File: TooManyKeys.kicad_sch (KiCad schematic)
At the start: 5 parts, among them J1 LCD Conn (1x8 PicoBlade), J2 BOOSTIER, SW1 SW_SPDT, SW2 SW_RST, U1 Nice_Nano_V2

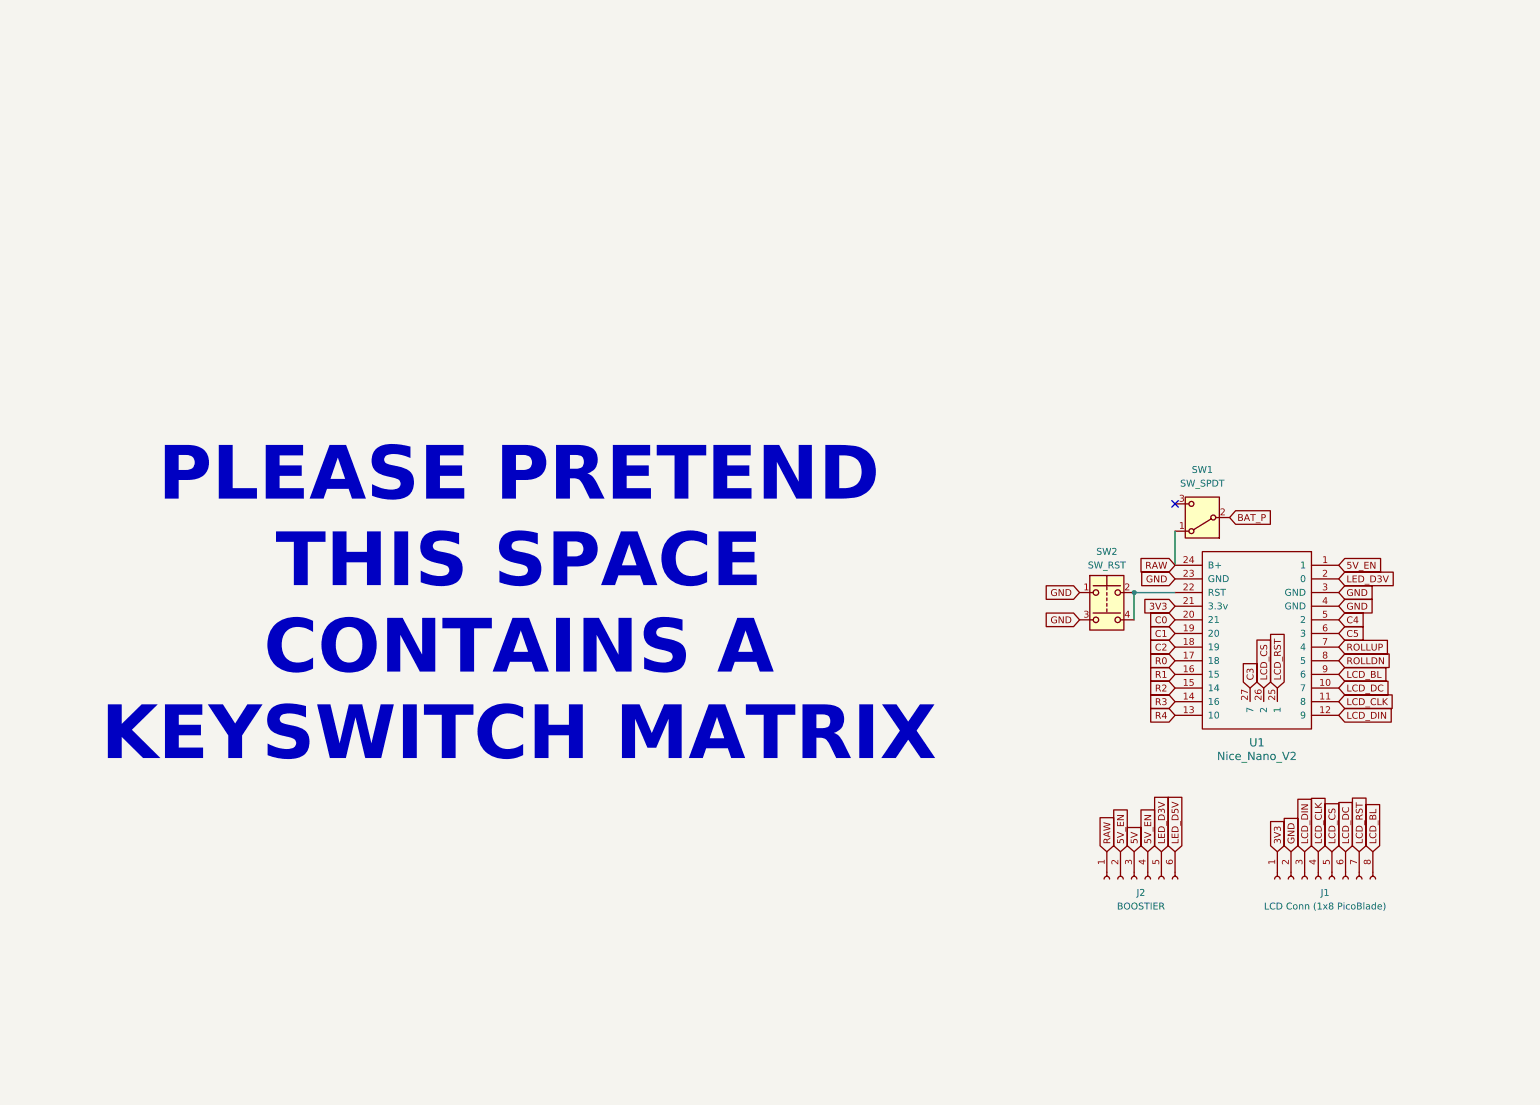
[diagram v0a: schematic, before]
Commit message: Finish schematic. Partial routing draft. Minor changes to via sizes in ergogen.
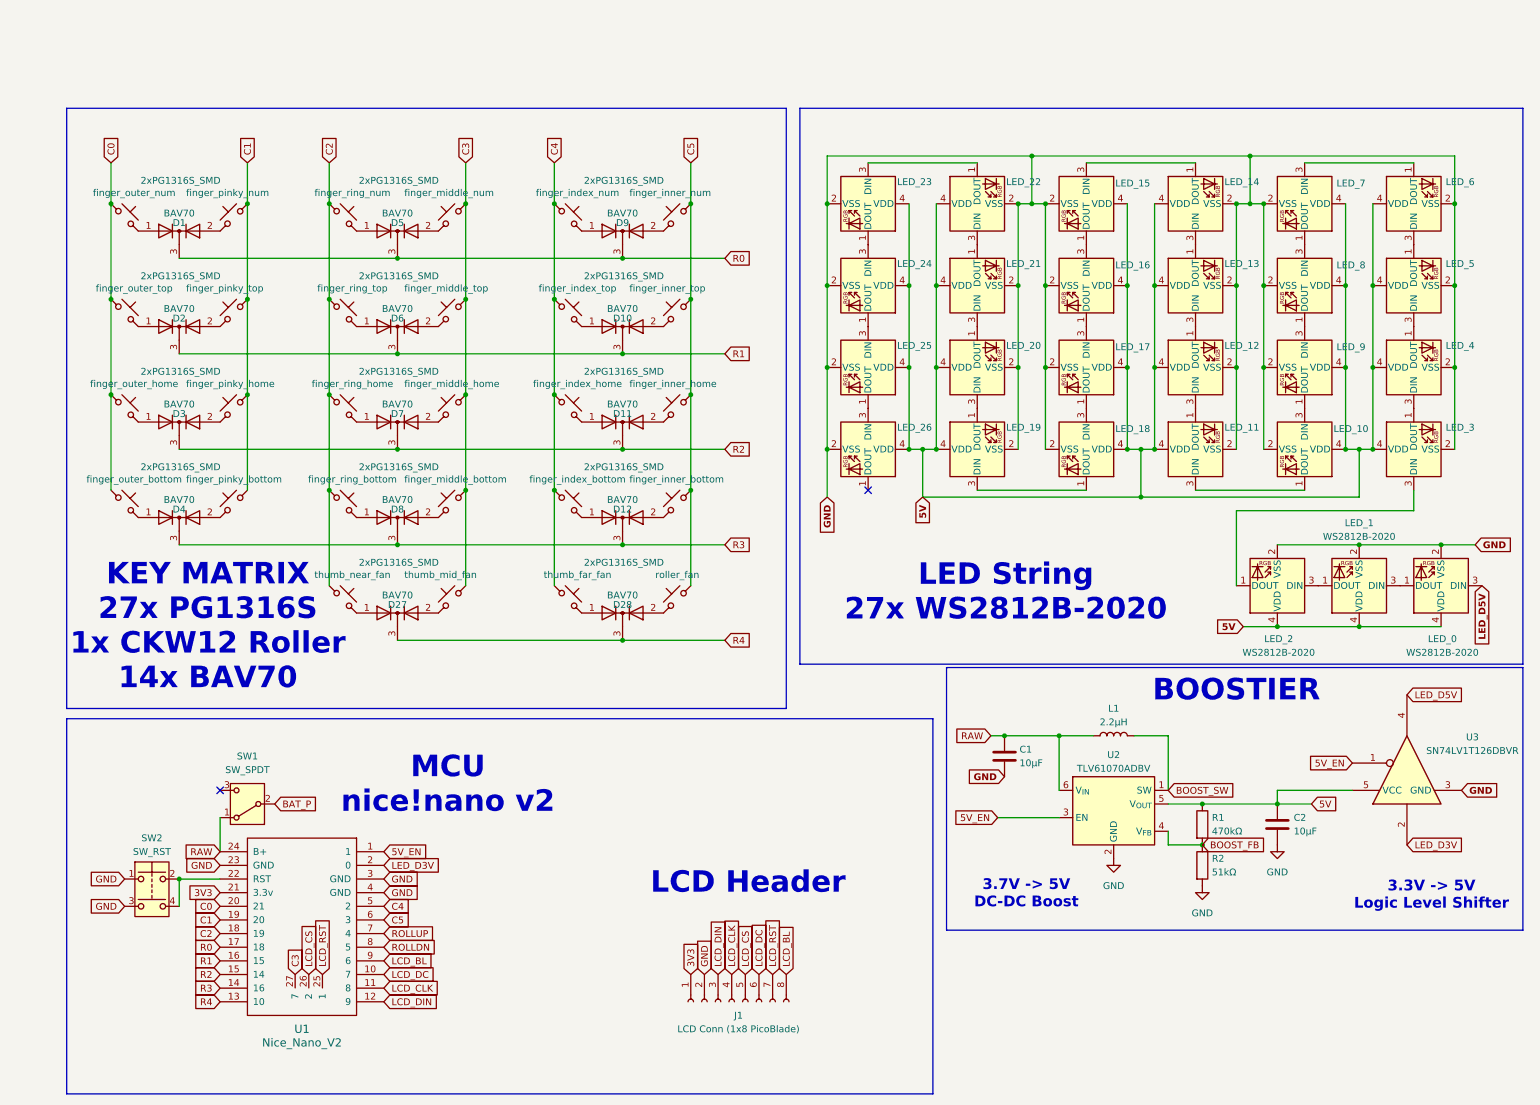
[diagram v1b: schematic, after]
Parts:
- removed J2: BOOSTIER, symbol Connector:Conn_01x06_Socket
- added C1, C2: 10μF, Capacitor_SMD:C_0603_1608Metric, symbol Device:C
- added D1, D10, D11, D12, D2, D27, D28, D3, D4, D5, D6, D7, D8, D9: BAV70, Package_TO_SOT_SMD:SOT-23, symbol Diode:BAV70
- added L1: 2.2μH, huntercook:L_CJIANG_FTC404030S_4.1x4.1x3.0_SMD, symbol Device:L
- added LED_0, LED_1, LED_10, LED_11, LED_12, LED_13, LED_14, LED_15, LED_16, LED_17, LED_18, LED_19, LED_2, LED_20, LED_21, LED_22, LED_23, LED_24, LED_25, LED_26, LED_3, LED_4, LED_5, LED_6, LED_7, LED_8, LED_9: WS2812B-2020, LED_SMD:LED_WS2812B-2020_PLCC4_2.0x2.0mm, symbol LED:WS2812B-2020
- added R1: 470kΩ, Resistor_SMD:R_0603_1608Metric, symbol Device:R
- added R2: 51kΩ, Resistor_SMD:R_0603_1608Metric, symbol Device:R
- added U2: TLV61070ADBV, Package_TO_SOT_SMD:SOT-23-6, symbol Regulator_Switching:TLV61070ADBV
- added U3: SN74LV1T126DBVR, Package_TO_SOT_SMD:SOT-23-5, symbol 74xGxx:SN74LVC1G125DBV
- added finger_index_bottom, finger_index_home, finger_index_num, finger_index_top, finger_outer_bottom, finger_outer_home, finger_outer_num, finger_outer_top, finger_ring_bottom, finger_ring_home, finger_ring_num, finger_ring_top, thumb_far_fan, thumb_near_fan: 2xPG1316S_SMD, PCM_marbastlib-choc:SW_choc_v1_1u, symbol marbastlib-choc:choc_v1_SW_solder
- added finger_inner_bottom, finger_inner_home, finger_inner_num, finger_inner_top, finger_middle_bottom, finger_middle_home, finger_middle_num, finger_middle_top, finger_pinky_bottom, finger_pinky_home, finger_pinky_num, finger_pinky_top, roller_fan, thumb_mid_fan: PG1316S_SMD, PCM_marbastlib-choc:SW_choc_v1_1u, symbol marbastlib-choc:choc_v1_SW_solder
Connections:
- net 5V: now also C2.1, LED_0.4 (VDD), LED_1.4 (VDD), LED_10.4 (VDD), LED_11.4 (VDD), LED_12.4 (VDD), LED_13.4 (VDD), LED_14.4 (VDD), LED_15.4 (VDD), LED_16.4 (VDD), LED_17.4 (VDD), LED_18.4 (VDD), LED_19.4 (VDD), LED_2.4 (VDD), LED_20.4 (VDD), LED_21.4 (VDD), LED_22.4 (VDD), LED_23.4 (VDD), LED_24.4 (VDD), LED_25.4 (VDD), LED_26.4 (VDD), LED_3.4 (VDD), LED_4.4 (VDD), LED_5.4 (VDD), LED_6.4 (VDD), LED_7.4 (VDD), LED_8.4 (VDD), LED_9.4 (VDD), R1.1, U2.5 (V_{OUT}), U3.5 (VCC)
- net 5V_EN: now also U2.3 (EN), U3.1
- net C0: now also finger_outer_bottom.1, finger_outer_home.1, finger_outer_num.1, finger_outer_top.1
- net C1: now also finger_pinky_bottom.2, finger_pinky_home.2, finger_pinky_num.2, finger_pinky_top.2
- net C2: now also finger_ring_bottom.1, finger_ring_home.1, finger_ring_num.1, finger_ring_top.1, thumb_near_fan.1
- net C3: now also finger_middle_bottom.2, finger_middle_home.2, finger_middle_num.2, finger_middle_top.2, thumb_mid_fan.2
- net C4: now also finger_index_bottom.1, finger_index_home.1, finger_index_num.1, finger_index_top.1, thumb_far_fan.1
- net C5: now also finger_inner_bottom.2, finger_inner_home.2, finger_inner_num.2, finger_inner_top.2, roller_fan.2
- net GND: now also C1.2, C2.2, LED_0.2 (VSS), LED_1.2 (VSS), LED_10.2 (VSS), LED_11.2 (VSS), LED_12.2 (VSS), LED_13.2 (VSS), LED_14.2 (VSS), LED_15.2 (VSS), LED_16.2 (VSS), LED_17.2 (VSS), LED_18.2 (VSS), LED_19.2 (VSS), LED_2.2 (VSS), LED_20.2 (VSS), LED_21.2 (VSS), LED_22.2 (VSS), LED_23.2 (VSS), LED_24.2 (VSS), LED_25.2 (VSS), LED_26.2 (VSS), LED_3.2 (VSS), LED_4.2 (VSS), LED_5.2 (VSS), LED_6.2 (VSS), LED_7.2 (VSS), LED_8.2 (VSS), LED_9.2 (VSS), R2.2, U2.2 (GND), U3.3 (GND)
- net LED_D3V: now also U3.2
- net LED_D5V: now also LED_0.3 (DIN), U3.4
- net R0: now also D1.3 (K), D5.3 (K), D9.3 (K)
- net R1: now also D10.3 (K), D2.3 (K), D6.3 (K)
- net R2: now also D11.3 (K), D3.3 (K), D7.3 (K)
- net R3: now also D12.3 (K), D4.3 (K), D8.3 (K)
- net R4: now also D27.3 (K), D28.3 (K)
- net RAW: now also C1.1, L1.1, U2.6 (V_{IN})
- new net: D27.2 (A), thumb_mid_fan.1
- new net: D12.1 (A), finger_index_bottom.2
- new net: LED_19.1 (DOUT), LED_20.3 (DIN)
- new net: LED_18.1 (DOUT), LED_19.3 (DIN)
- new net: LED_11.1 (DOUT), LED_12.3 (DIN)
- new net: LED_10.1 (DOUT), LED_11.3 (DIN)
- new net: D7.1 (A), finger_ring_home.2
- new net: LED_6.1 (DOUT), LED_7.3 (DIN)
- new net: LED_5.1 (DOUT), LED_6.3 (DIN)
- new net: D2.1 (A), finger_outer_top.2
- new net: D2.2 (A), finger_pinky_top.1
- new net: D1.1 (A), finger_outer_num.2
- new net: D1.2 (A), finger_pinky_num.1
- new net: D3.1 (A), finger_outer_home.2
- new net: D3.2 (A), finger_pinky_home.1
- new net: LED_20.1 (DOUT), LED_21.3 (DIN)
- new net: D11.1 (A), finger_index_home.2
- new net: LED_12.1 (DOUT), LED_13.3 (DIN)
- new net: LED_1.1 (DOUT), LED_2.3 (DIN)
- new net: LED_0.1 (DOUT), LED_1.3 (DIN)
- new net: D12.2 (A), finger_inner_bottom.1
- new net: D8.1 (A), finger_ring_bottom.2
- new net: D8.2 (A), finger_middle_bottom.1
- new net: D10.1 (A), finger_index_top.2
- new net: LED_21.1 (DOUT), LED_22.3 (DIN)
- new net: D9.1 (A), finger_index_num.2
- new net: D7.2 (A), finger_middle_home.1
- new net: LED_4.1 (DOUT), LED_5.3 (DIN)
- new net: LED_3.1 (DOUT), LED_4.3 (DIN)
- new net: LED_22.1 (DOUT), LED_23.3 (DIN)
- new net: LED_24.1 (DOUT), LED_25.3 (DIN)
- new net: LED_23.1 (DOUT), LED_24.3 (DIN)
- new net: D9.2 (A), finger_inner_num.1
- new net: LED_2.1 (DOUT), LED_3.3 (DIN)
- new net: D4.1 (A), finger_outer_bottom.2
- new net: D28.1 (A), thumb_far_fan.2
- new net: D28.2 (A), roller_fan.1
- new net: D6.1 (A), finger_ring_top.2
- new net: LED_10.3 (DIN), LED_9.1 (DOUT)
- new net: LED_8.1 (DOUT), LED_9.3 (DIN)
- new net: D11.2 (A), finger_inner_home.1
- new net: D27.1 (A), thumb_near_fan.2
- new net: D5.1 (A), finger_ring_num.2
- new net: D5.2 (A), finger_middle_num.1
- new net: LED_7.1 (DOUT), LED_8.3 (DIN)
- new net: D4.2 (A), finger_pinky_bottom.1
- new net: LED_15.1 (DOUT), LED_16.3 (DIN)
- new net: LED_14.1 (DOUT), LED_15.3 (DIN)
- new net: LED_25.1 (DOUT), LED_26.3 (DIN)
- new net: LED_17.1 (DOUT), LED_18.3 (DIN)
- new net: LED_16.1 (DOUT), LED_17.3 (DIN)
- new net: D10.2 (A), finger_inner_top.1
- new net: D6.2 (A), finger_middle_top.1
- new net: LED_13.1 (DOUT), LED_14.3 (DIN)
- new net BOOST_FB: R1.2, R2.1, U2.4 (V_{FB})
- new net BOOST_SW: L1.2, U2.1 (SW)
- no-connect marks 1 -> 2
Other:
- note added: "3.3V -> 5V Logic Level Shifter"
- note added: "3.7V -> 5V DC-DC Boost"
- note added: "BOOSTIER"
- note added: "KEY MATRIX 27x PG1316S 1x CKW12 Roller 14x BAV70"
- note added: "LCD Header"
- note added: "LED String 27x WS2812B-2020"
- note added: "MCU nice!nano v2"
- note removed: "PLEASE PRETEND THIS SPACE CONTAINS A KEYSWITCH MATRIX"
- moved on the sheet: J1, SW1, SW2, U1

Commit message: Redo schematic references to match ergogen, work on connecting sch and pcb.
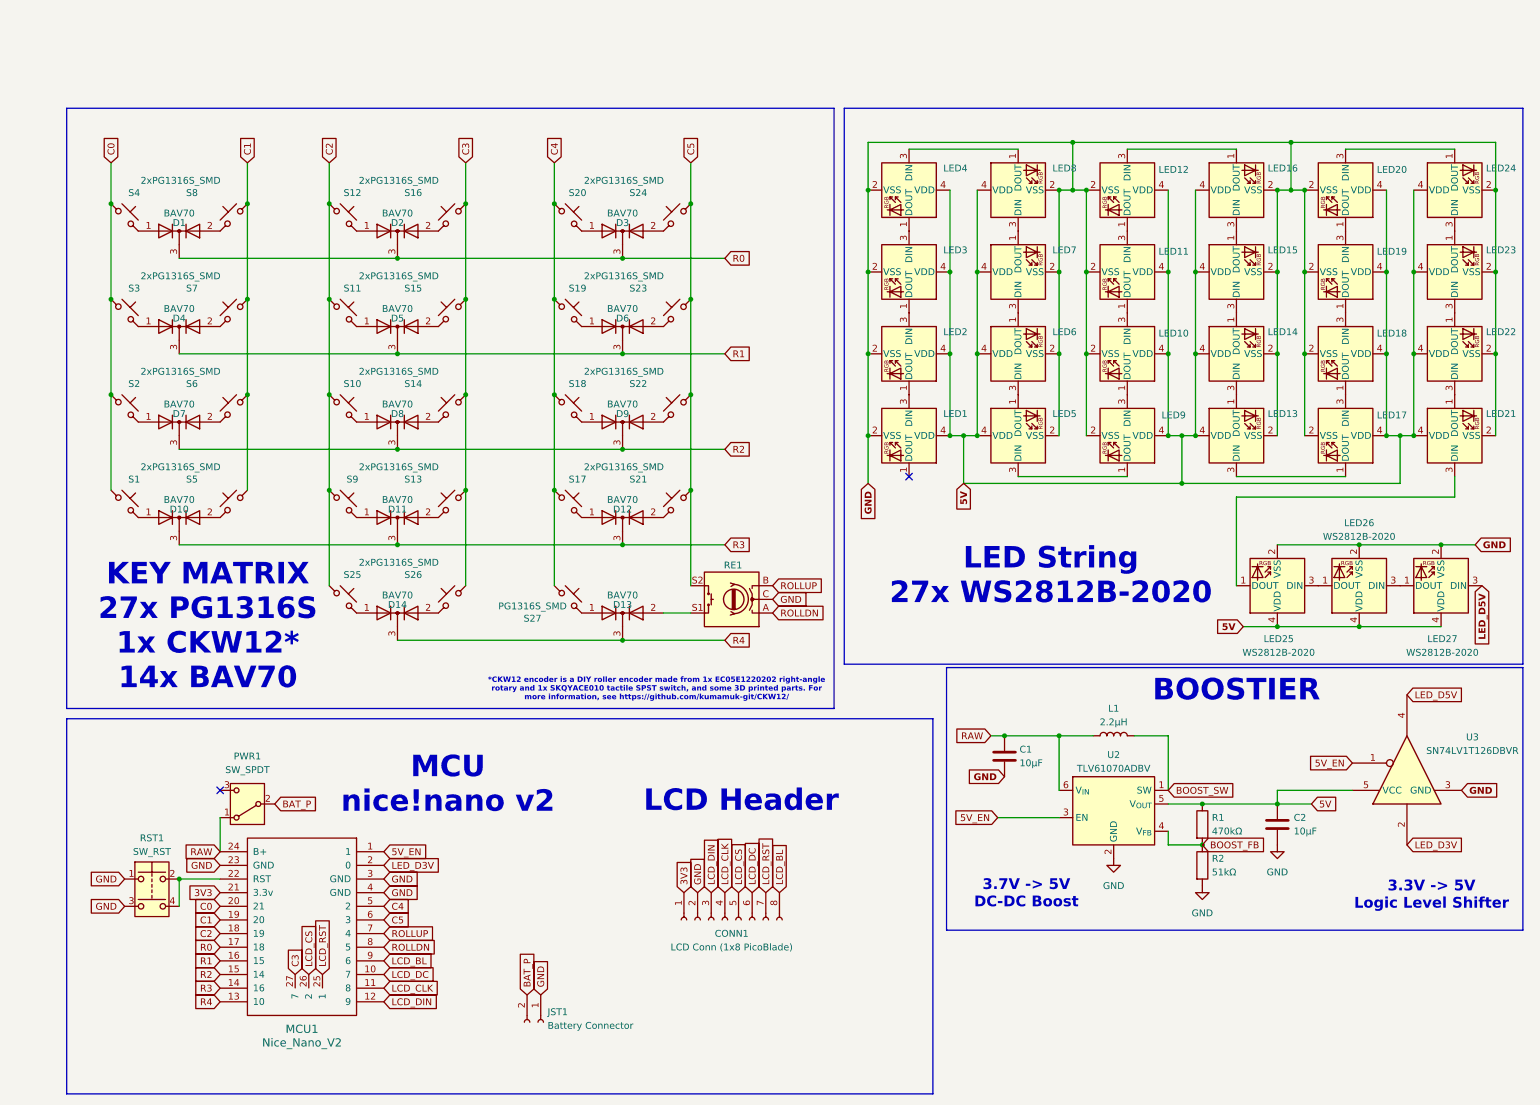
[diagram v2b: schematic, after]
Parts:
- removed roller_fan: PG1316S_SMD, PCM_marbastlib-choc:SW_choc_v1_1u, symbol marbastlib-choc:choc_v1_SW_solder
- added JST1: Battery Connector, symbol Connector:Conn_01x02_Socket
- added SW3: RE1, symbol Device:RotaryEncoder_Switch
- S27: renamed from thumb_far_fan; value 2xPG1316S_SMD -> PG1316S_SMD
- renumbered J1 to CONN1, D4 to D10, D8 to D11, D28 to D13, D27 to D14, D5 to D2, D9 to D3, D2 to D4, D6 to D5, D10 to D6, D3 to D7, D7 to D8, D11 to D9, LED_26 to LED1, LED_17 to LED10, LED_16 to LED11, LED_15 to LED12, LED_11 to LED13, LED_12 to LED14, LED_13 to LED15, LED_14 to LED16, LED_10 to LED17, LED_9 to LED18, LED_8 to LED19, LED_25 to LED2, LED_7 to LED20, LED_3 to LED21, LED_4 to LED22, LED_5 to LED23, LED_6 to LED24, LED_2 to LED25, LED_1 to LED26, LED_0 to LED27, LED_24 to LED3, LED_23 to LED4, LED_19 to LED5, LED_20 to LED6, LED_21 to LED7, LED_22 to LED8, LED_18 to LED9, U1 to MCU1, SW1 to PWR1, SW2 to RST1, finger_outer_bottom to S1, finger_ring_home to S10, finger_ring_top to S11, finger_ring_num to S12, finger_middle_bottom to S13, finger_middle_home to S14, finger_middle_top to S15, finger_middle_num to S16, finger_index_bottom to S17, finger_index_home to S18, finger_index_top to S19, finger_outer_home to S2, finger_index_num to S20, finger_inner_bottom to S21, finger_inner_home to S22, finger_inner_top to S23, finger_inner_num to S24, thumb_near_fan to S25, thumb_mid_fan to S26, finger_outer_top to S3, finger_outer_num to S4, finger_pinky_bottom to S5, finger_pinky_home to S6, finger_pinky_top to S7, finger_pinky_num to S8, finger_ring_bottom to S9
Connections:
- net BAT_P: now also JST1.2 (Pin_2)
- net C5: now also SW3.S2
- net GND: now also JST1.1 (Pin_1), SW3.C
- net ROLLDN: now also SW3.A
- net ROLLUP: now also SW3.B
- net at D13.2 (A): now also SW3.S1
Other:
- note added: "*CKW12 encoder is a DIY roller encoder made from 1x EC05E1220202 right-angle rotary and 1x SKQYACE010 tactile SPST switch, and some 3D printed parts. For more information, see https://github.com/kumamuk-git/CKW12/"
- note added: "KEY MATRIX 27x PG1316S 1x CKW12* 14x BAV70"
- note removed: "KEY MATRIX 27x PG1316S 1x CKW12 Roller 14x BAV70"
- moved on the sheet: CONN1, LED1, LED10, LED11, LED12, LED13, LED14, LED15, LED16, LED17, LED18, LED19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

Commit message: Integrate schematic with PCB
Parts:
- CONN1: value LCD Conn (1x8 PicoBlade) -> ~; footprint (none) -> Molex_PicoBlade_53261-0871_1x08-1MP_P1.25mm_Horizontal
- D1, D10, D11, D12, D13, D14, D2, D3, D4, D5, D6, D7, D8, D9: footprint Package_TO_SOT_SMD:SOT-23 -> BAV70 SOT23
- JST1: value Battery Connector -> ~; footprint (none) -> ceoloide:battery_connector_jst_ph_2
- LED1, LED10, LED11, LED12, LED13, LED14, LED15, LED16, LED17, LED18, LED19, LED2, LED20, LED21, LED22, LED23, LED24, LED25, LED26, LED27, LED3, LED4, LED5, LED6, LED7, LED8, LED9: value WS2812B-2020 -> ~; footprint LED_SMD:LED_WS2812B-2020_PLCC4_2.0x2.0mm -> LED_WS2812B-2020_PLCC4_2.0x2.0mm
- MCU1: value Nice_Nano_V2 -> ~; footprint ScottoKeebs_MCU:Nice_Nano_V2 -> ceoloide:mcu_nice_nano; now left out of the parts list
- PWR1: value SW_SPDT -> ~; footprint (none) -> ceoloide:power_switch_smd_side
- RE1: renamed from SW3; value RE1 -> (none); footprint (none) -> CKW12
- RST1: value SW_RST -> ~; footprint (none) -> ceoloide:reset_switch_smd_side
- S1, S10, S11, S12, S17, S18, S19, S2, S20, S25, S3, S4, S9: value 2xPG1316S_SMD -> ~; footprint PCM_marbastlib-choc:SW_choc_v1_1u -> PG1316S
- S13, S14, S15, S16, S21, S22, S23, S24, S26, S27, S5, S6, S7, S8: value PG1316S_SMD -> ~; footprint PCM_marbastlib-choc:SW_choc_v1_1u -> PG1316S
